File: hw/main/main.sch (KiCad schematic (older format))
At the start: 22 parts, among them U1 MCP1703A-3302, U2 STM32L011D3, X1 01x04_P2.54mm_Hor, X2 01x04_P2.54mm_Hor

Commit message: wip
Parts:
- removed C5: 100n_50V, Capacitor_SMD:C_0805_2012Metric, symbol _C_0805:100n_50V
- removed D2: TS4148RYG, Diode_SMD:D_0805_2012Metric, symbol _Diode:TS4148RYG
- removed R2, R6: ?, Resistor_SMD:R_0805_2012Metric, symbol _R_0805:?
- added C?: CP, symbol Device:CP
- added D?: SS14HE, Diode_SMD:D_0805_2012Metric, symbol _Diode_Schottky:SS14HE
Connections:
- net LPUART1_RX: now also R3.2
- net GPIO_EXTI15: no longer names the net of U2.3 (PC15)
- net GPIO_EXTI15: no longer R3.2
- net Vext: no longer names the net of D1.2 (A), X2.1 (Pin_1)
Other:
- moved on the sheet: C1, C2, C3, C4, C7, C8, D1, D3, R1, R3, R5, R7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

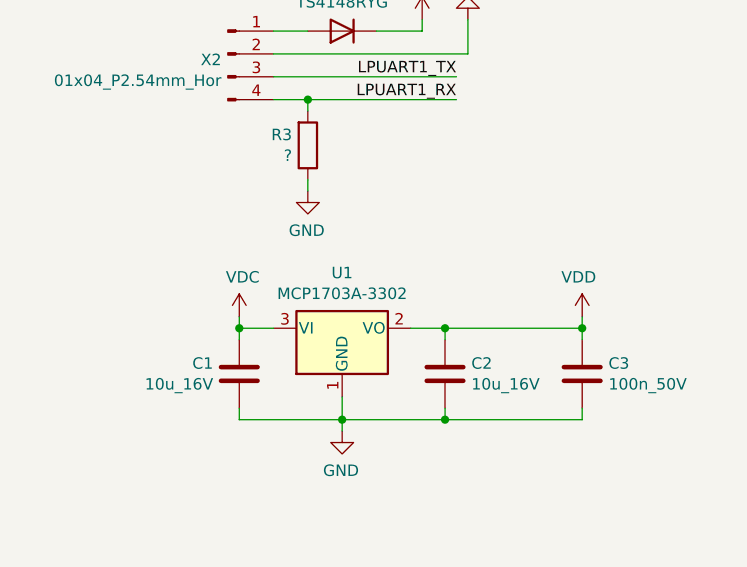
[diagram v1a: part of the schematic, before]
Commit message: Changed LDO output to 1.8V
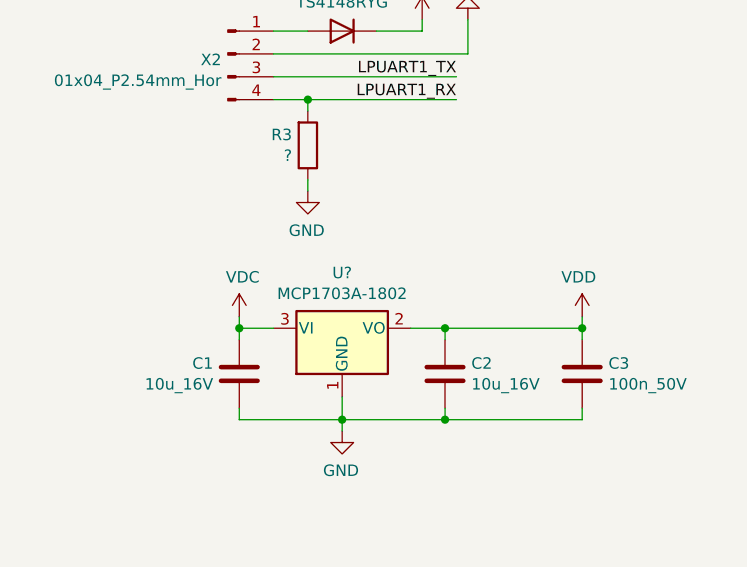
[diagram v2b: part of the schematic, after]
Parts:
- removed U1: MCP1703A-3302, Package_TO_SOT_SMD:SOT-23, symbol _Regulator_Linear:MCP1703A-3302
- added U?: MCP1703A-1802, Package_TO_SOT_SMD:SOT-23, symbol _Regulator_Linear:MCP1703A-1802
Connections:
- net GND: now also U?.1 (GND)
- net VDC: now also U?.3 (VI)
- net VDD: now also U?.2 (VO)
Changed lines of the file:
@@
-$EndComp
-$Comp
-L _Regulator_Linear:MCP1703A-3302 U1
-U 1 1 5E85204B
-P 1850 2850
-F 0 "U1" H 1850 3092 50  0000 C CNN
-F 1 "MCP1703A-3302" H 1850 3001 50  0000 C CNN
-F 2 "Package_TO_SOT_SMD:SOT-23" H 1850 3050 50  0001 C CNN
-F 3 "http://ww1.microchip.com/downloads/en/DeviceDoc/20005122B.pdf" H 1850 2800 50  0001 C CNN
-F 4 "Microchip Technology" H 1950 3050 50  0001 C CNN "MF"
-F 5 "MCP1703Ax-3302E/CB" H 2050 3150 50  0001 C CNN "MPN"
-F 6 "-" H 2150 3250 50  0001 C CNN "OC_CONRAD"
-F 7 "-" H 2250 3350 50  0001 C CNN "OC_FARNELL"
-F 8 "579-MCP1703AT3302ECB" H 2350 3450 50  0001 C CNN "OC_MOUSER"
-F 9 "-" H 2450 3550 50  0001 C CNN "OC_REICHELT"
-F 10 "114" H 2550 3650 50  0001 C CNN "ID"
-F 11 "Low Quiescent Current LDO Regulator, 3.3V, 250mA, Vin<=16V, SOT-23" H 2650 3750 50  0001 C CNN "Description"
-	1    1850 2850
-	1    0    0    -1
 $EndComp
 $Comp
@@
 	1    0    0    -1
 $EndComp
+$Comp
+L _Regulator_Linear:MCP1703A-1802 U?
+U 1 1 5E8CE8B9
+P 1850 2850
+F 0 "U?" H 1850 3092 50  0000 C CNN
+F 1 "MCP1703A-1802" H 1850 3001 50  0000 C CNN
+F 2 "Package_TO_SOT_SMD:SOT-23" H 1850 3050 50  0001 C CNN
+F 3 "http://ww1.microchip.com/downloads/en/DeviceDoc/20005122B.pdf" H 1850 2800 50  0001 C CNN
+F 4 "Microchip Technology" H 1950 3050 50  0001 C CNN "MF"
+F 5 "MCP1703Ax-1802E/CB" H 2050 3150 50  0001 C CNN "MPN"
+F 6 "-" H 2150 3250 50  0001 C CNN "OC_CONRAD"
+F 7 "-" H 2250 3350 50  0001 C CNN "OC_FARNELL"
+F 8 "579-MCP1703AT1802ECB" H 2350 3450 50  0001 C CNN "OC_MOUSER"
+F 9 "-" H 2450 3550 50  0001 C CNN "OC_REICHELT"
+F 10 "128" H 2550 3650 50  0001 C CNN "ID"
+F 11 "Low Quiescent Current LDO Regulator, 1.8V, 250mA, Vin<=16V, SOT-23" H 2650 3750 50  0001 C CNN "Description"
+	1    1850 2850
+	1    0    0    -1
+$EndComp

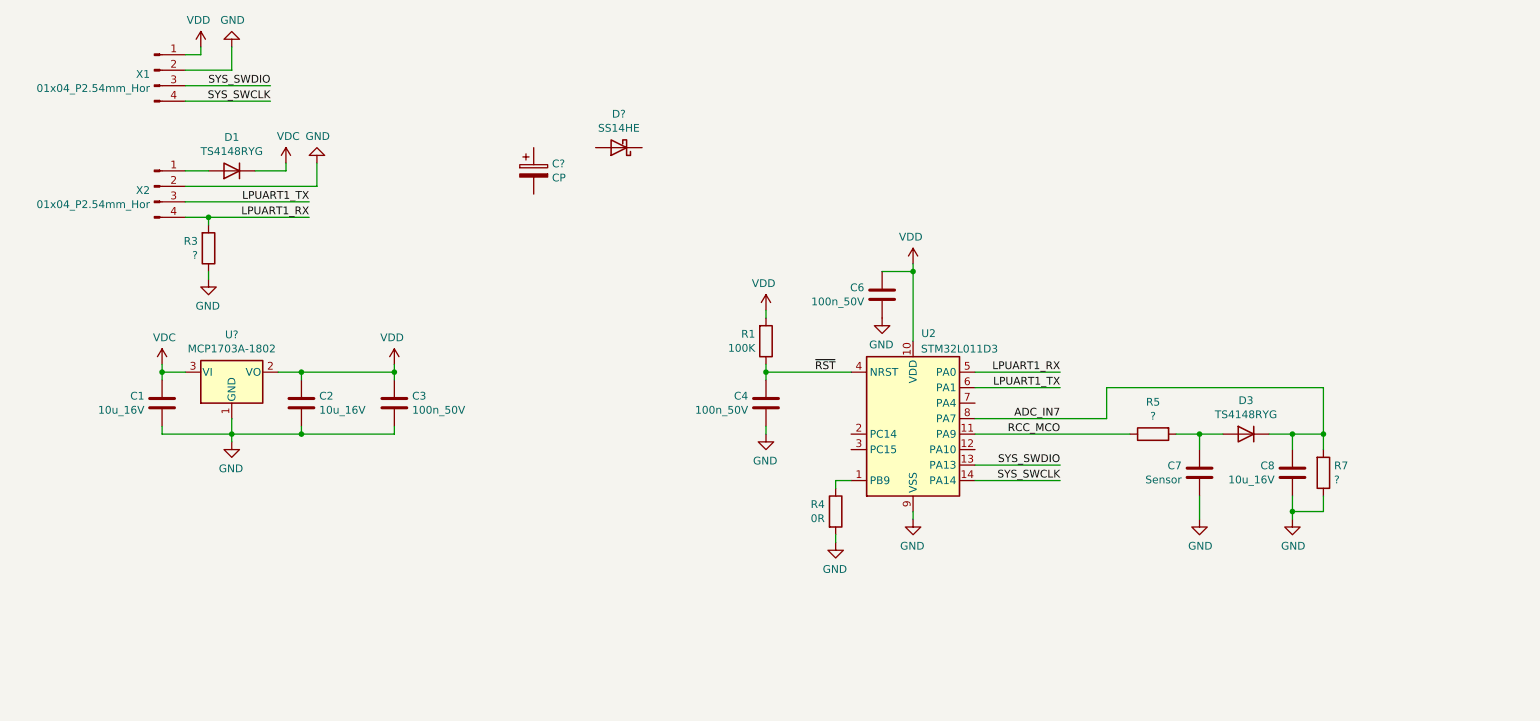
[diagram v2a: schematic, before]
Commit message: Added timer 555 to measure sensor capacity
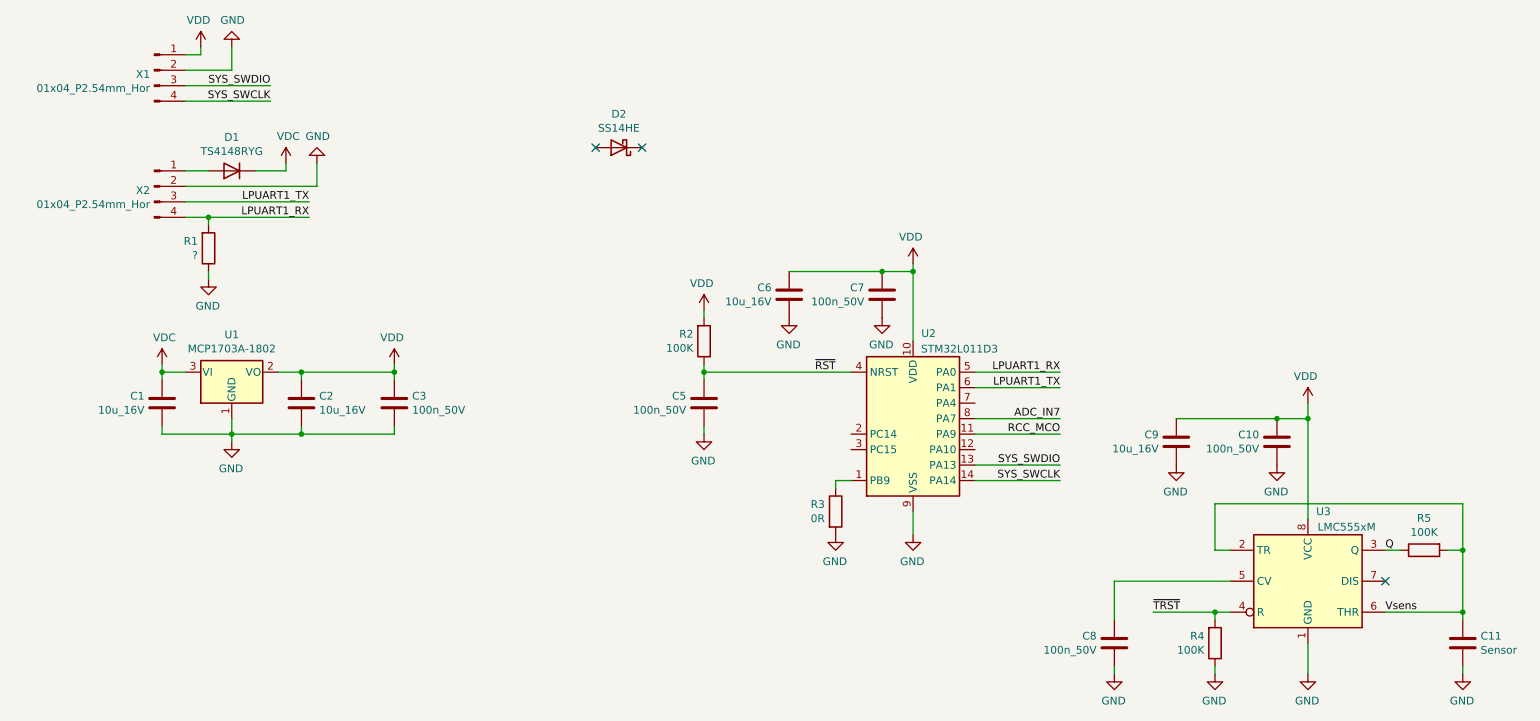
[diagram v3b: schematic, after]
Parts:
- removed C8: 10u_16V, Capacitor_SMD:C_0805_2012Metric, symbol _C_0805:10u_16V
- removed C?: CP, symbol Device:CP
- removed D3: TS4148RYG, Diode_SMD:D_0805_2012Metric, symbol _Diode:TS4148RYG
- removed R5, R7: ?, Resistor_SMD:R_0805_2012Metric, symbol _R_0805:?
- added C10, C8: 100n_50V, Capacitor_SMD:C_0805_2012Metric, symbol _C_0805:100n_50V
- added C6, C9: 10u_16V, Capacitor_SMD:C_0805_2012Metric, symbol _C_0805:10u_16V
- added R4, R5: 100K, Resistor_SMD:R_0805_2012Metric, symbol _R_0805:100K
- added U3: LMC555xM, Package_SO:SOIC-8_3.9x4.9mm_P1.27mm, symbol _Timer:LMC555xM
- gave numbers to parts that had none: 2
- renumbered C7 to C11, C4 to C5, C6 to C7, R3 to R1, R1 to R2, R4 to R3
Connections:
- net GND: now also C10.2, C6.2, C8.2, C9.2, R4.1, U3.1 (GND)
- net VDD: now also C10.1, C6.1, C9.1, U3.8 (VCC)
- net Vsens: now reaches C11.1
- net Vsens: now also R5.2, U3.2 (TR), U3.6 (THR)
- new net: C8.1, U3.5 (CV)
- new net Q: R5.1, U3.3 (Q)
- new net ~TRST: R4.2, U3.4 (R)
- no-connect marks 0 -> 3
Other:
- moved on the sheet: C11, C5, R2
